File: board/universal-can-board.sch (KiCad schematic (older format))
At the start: 57 parts, among them IC1 ATMEGA328P-A, P1 USB_OTG, U1 FT232RL

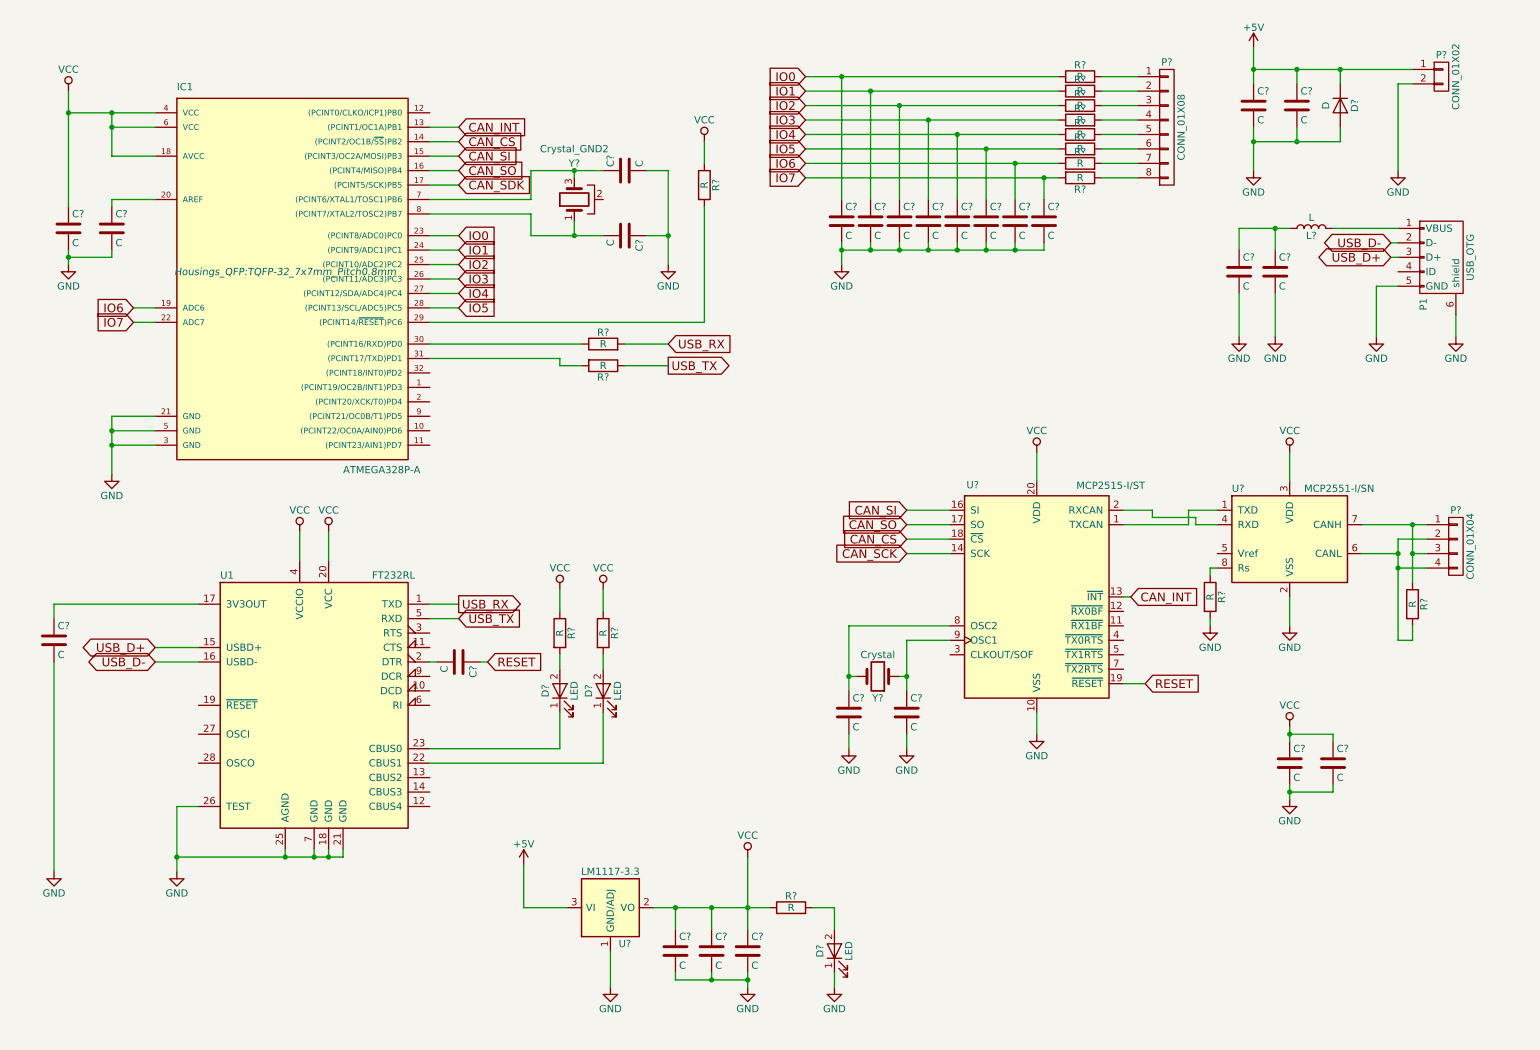
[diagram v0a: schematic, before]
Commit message: Added values to the board schematic.
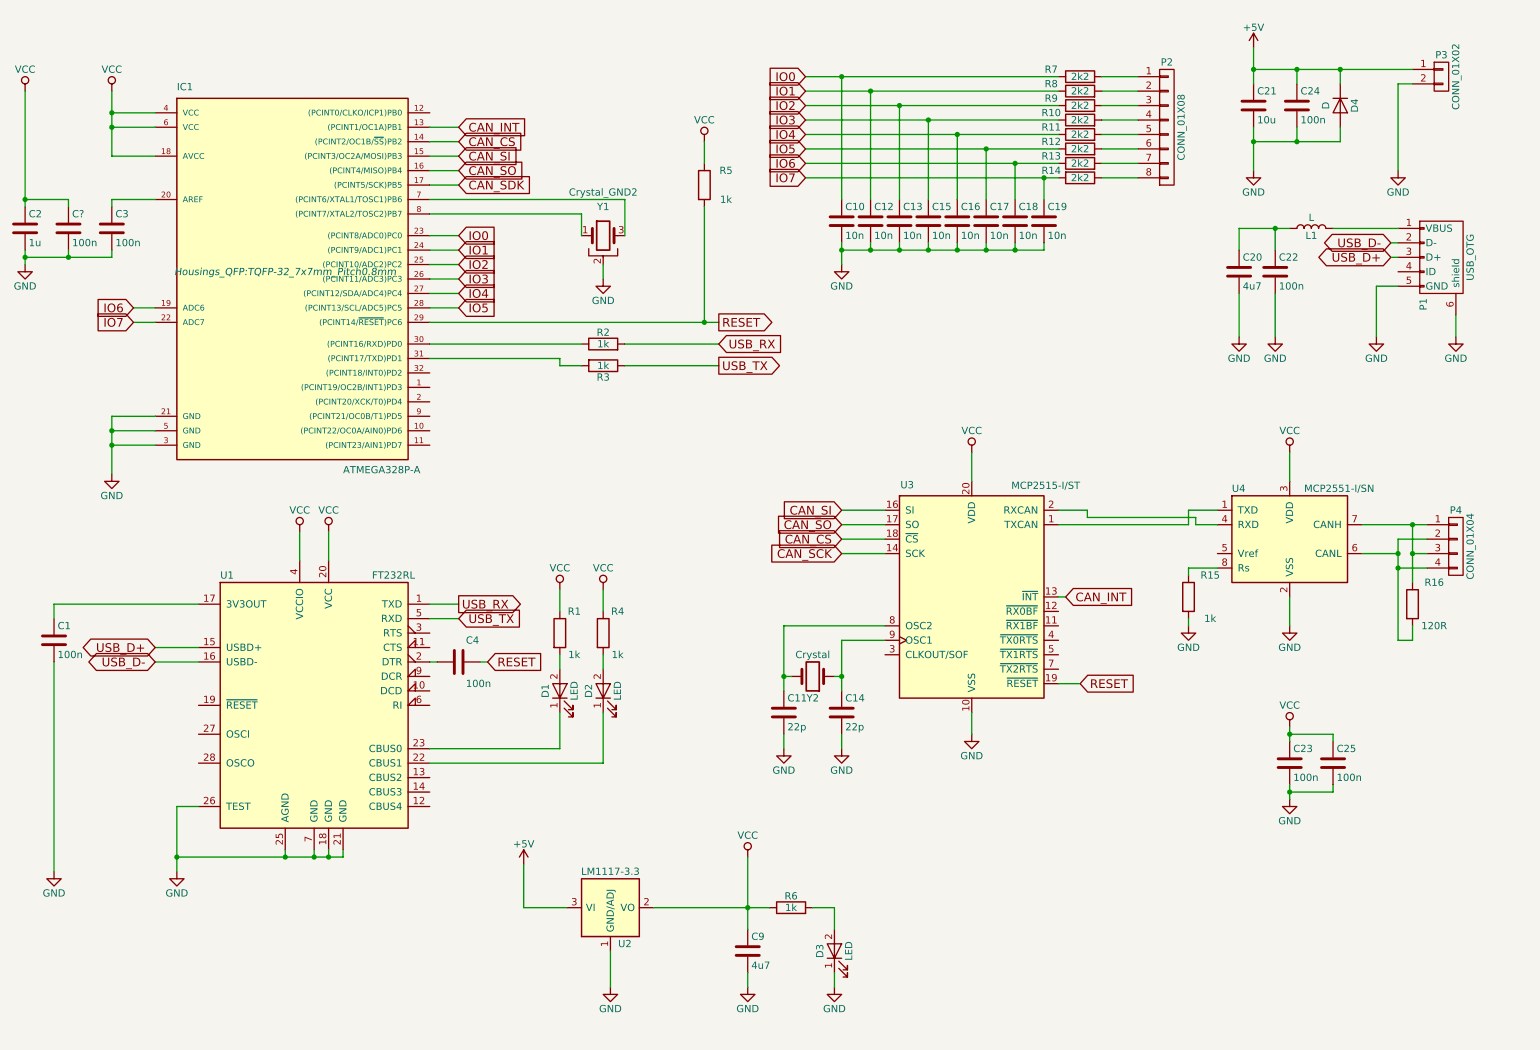
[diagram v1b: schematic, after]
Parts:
- removed C? (x4): C, symbol C
- added C?: 100n, symbol C
- C1, C22, C23, C24, C25, C3, C4: renamed from C?; value C -> 100n
- C10, C12, C13, C15, C16, C17, C18, C19: renamed from C?; value C -> 10n
- C11, C14: renamed from C?; value C -> 22p
- C2: renamed from C?; value C -> 1u
- C20, C9: renamed from C?; value C -> 4u7
- C21: renamed from C?; value C -> 10u
- R1, R15, R2, R3, R4, R5, R6: renamed from R?; value R -> 1k
- R10, R11, R12, R13, R14, R7, R8, R9: renamed from R?; value R -> 2k2
- R16: renamed from R?; value R -> 120R
- gave numbers to parts that had none: 13
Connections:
- net GND: now also Y1.2, C?.2
- net RESET: now also IC1.29 ((PCINT14/~RESET~)PC6), R5.2
- net VCC: now also C?.1
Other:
- moved on the sheet: C11, C14, C2, R15, U3, Y1, Y2

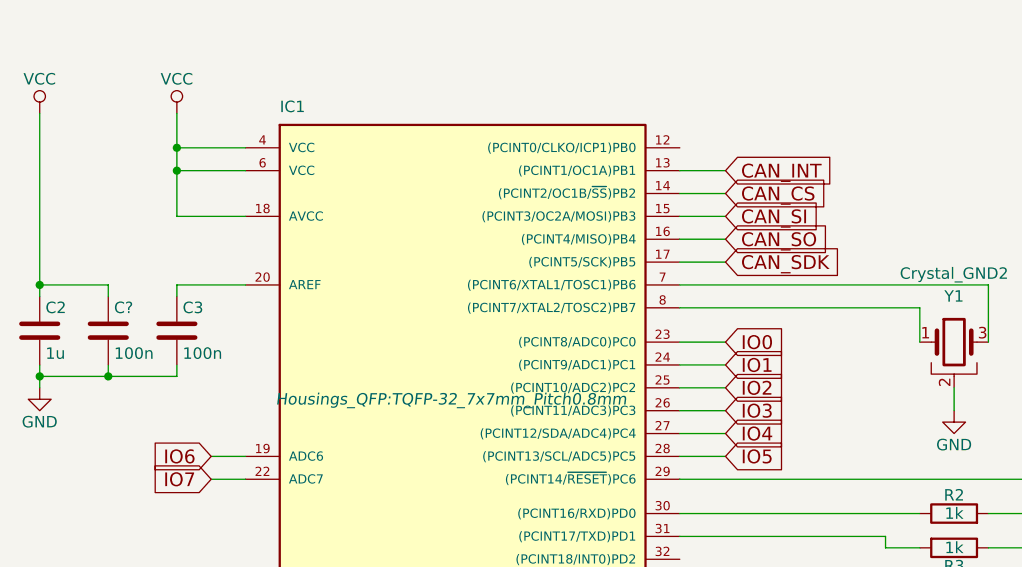
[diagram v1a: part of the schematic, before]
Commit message: Removed conflicts in board schematic.
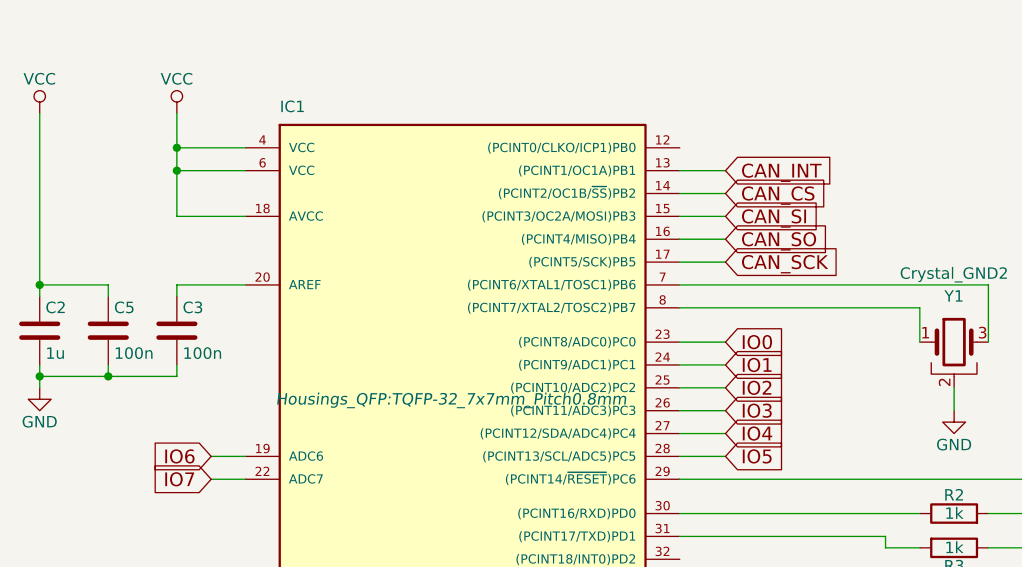
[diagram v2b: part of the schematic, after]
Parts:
- gave numbers to parts that had none: 1
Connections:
- net CAN_SDK is gone; now on net CAN_SCK: IC1.17 ((PCINT5/SCK)PB5)
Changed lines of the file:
@@
 $EndComp
 $Comp
-L GND #PWR4
+L GND #PWR01
 U 1 1 5A6CF0D9
 P 1350 3700
-F 0 "#PWR4" H 1350 3450 50  0001 C CNN
+F 0 "#PWR01" H 1350 3450 50  0001 C CNN
 F 1 "GND" H 1350 3550 50  0000 C CNN
 F 2 "" H 1350 3700 50  0000 C CNN
@@
 	750  1050 750  1850
 $Comp
-L GND #PWR3
+L GND #PWR02
 U 1 1 5A6CF36D
 P 750 2250
-F 0 "#PWR3" H 750 2000 50  0001 C CNN
+F 0 "#PWR02" H 750 2000 50  0001 C CNN
 F 1 "GND" H 750 2100 50  0000 C CNN
 F 2 "" H 750 2250 50  0000 C CNN
@@
 Connection ~ 750  2200
 $Comp
-L VCC #PWR2
+L VCC #PWR03
 U 1 1 5A6CF8D1
 P 750 1050
-F 0 "#PWR2" H 750 900 50  0001 C CNN
+F 0 "#PWR03" H 750 900 50  0001 C CNN
 F 1 "VCC" H 750 1200 50  0000 C CNN
 F 2 "" H 750 1050 50  0000 C CNN
@@
 	5450 1850 5450 2650
 $Comp
-L VCC #PWR13
+L VCC #PWR04
 U 1 1 5A6CFAE4
 P 5450 1400
-F 0 "#PWR13" H 5450 1250 50  0001 C CNN
+F 0 "#PWR04" H 5450 1250 50  0001 C CNN
 F 1 "VCC" H 5450 1550 50  0000 C CNN
 F 2 "" H 5450 1400 50  0000 C CNN
@@
 $EndComp
 $Comp
-L GND #PWR11
+L GND #PWR05
 U 1 1 5A6D0725
 P 4800 7250
-F 0 "#PWR11" H 4800 7000 50  0001 C CNN
+F 0 "#PWR05" H 4800 7000 50  0001 C CNN
 F 1 "GND" H 4800 7100 50  0000 C CNN
 F 2 "" H 4800 7250 50  0000 C CNN
@@
 	4800 7250 4800 7000
 $Comp
-L +5V #PWR8
+L +5V #PWR06
 U 1 1 5A6D0796
 P 4200 6400
-F 0 "#PWR8" H 4200 6250 50  0001 C CNN
+F 0 "#PWR06" H 4200 6250 50  0001 C CNN
 F 1 "+5V" H 4200 6540 50  0000 C CNN
 F 2 "" H 4200 6400 50  0000 C CNN
@@
 	4200 6400 4200 6700
 $Comp
-L VCC #PWR14
+L VCC #PWR07
 U 1 1 5A6D09D0
 P 5750 6350
-F 0 "#PWR14" H 5750 6200 50  0001 C CNN
+F 0 "#PWR07" H 5750 6200 50  0001 C CNN
 F 1 "VCC" H 5750 6500 50  0000 C CNN
 F 2 "" H 5750 6350 50  0000 C CNN
@@
 Connection ~ 5750 6700
 Wire Wire Line
-	5100 6700 5900 6700
-Wire Wire Line
 	5750 7150 5750 7250
 $Comp
-L GND #PWR15
+L GND #PWR08
 U 1 1 5A6D0D86
 P 5750 7250
-F 0 "#PWR15" H 5750 7000 50  0001 C CNN
+F 0 "#PWR08" H 5750 7000 50  0001 C CNN
 F 1 "GND" H 5750 7100 50  0000 C CNN
 F 2 "" H 5750 7250 50  0000 C CNN
@@
 	6350 6700 6350 6850
 $Comp
-L GND #PWR16
+L GND #PWR09
 U 1 1 5A6D152D
 P 6350 7250
-F 0 "#PWR16" H 6350 7000 50  0001 C CNN
+F 0 "#PWR09" H 6350 7000 50  0001 C CNN
 F 1 "GND" H 6350 7100 50  0000 C CNN
 F 2 "" H 6350 7250 50  0000 C CNN
@@
 $EndComp
 $Comp
-L GND #PWR25
+L GND #PWR010
 U 1 1 5A6D1F72
 P 9250 1600
-F 0 "#PWR25" H 9250 1350 50  0001 C CNN
+F 0 "#PWR010" H 9250 1350 50  0001 C CNN
 F 1 "GND" H 9250 1450 50  0000 C CNN
 F 2 "" H 9250 1600 50  0000 C CNN
@@
 Connection ~ 9550 1400
 $Comp
-L GND #PWR32
+L GND #PWR011
 U 1 1 5A6D222F
 P 10250 1600
-F 0 "#PWR32" H 10250 1350 50  0001 C CNN
+F 0 "#PWR011" H 10250 1350 50  0001 C CNN
 F 1 "GND" H 10250 1450 50  0000 C CNN
 F 2 "" H 10250 1600 50  0000 C CNN
@@
 	10250 1000 10350 1000
 $Comp
-L +5V #PWR24
+L +5V #PWR012
 U 1 1 5A6D22D2
 P 9250 750
-F 0 "#PWR24" H 9250 600 50  0001 C CNN
+F 0 "#PWR012" H 9250 600 50  0001 C CNN
 F 1 "+5V" H 9250 890 50  0000 C CNN
 F 2 "" H 9250 750 50  0000 C CNN
@@
 	9800 2000 10250 2000
 $Comp
-L GND #PWR31
+L GND #PWR013
 U 1 1 5A6D5AAC
 P 10100 2750
-F 0 "#PWR31" H 10100 2500 50  0001 C CNN
+F 0 "#PWR013" H 10100 2500 50  0001 C CNN
 F 1 "GND" H 10100 2600 50  0000 C CNN
 F 2 "" H 10100 2750 50  0000 C CNN
@@
 	10650 2600 10650 2750
 $Comp
-L GND #PWR33
+L GND #PWR014
 U 1 1 5A6D5D80
 P 10650 2750
-F 0 "#PWR33" H 10650 2500 50  0001 C CNN
+F 0 "#PWR014" H 10650 2500 50  0001 C CNN
 F 1 "GND" H 10650 2600 50  0000 C CNN
 F 2 "" H 10650 2750 50  0000 C CNN
@@
 Connection ~ 9400 2000
 $Comp
-L GND #PWR26
+L GND #PWR015
 U 1 1 5A6D64CB
 P 9400 2750
-F 0 "#PWR26" H 9400 2500 50  0001 C CNN
+F 0 "#PWR015" H 9400 2500 50  0001 C CNN
 F 1 "GND" H 9400 2600 50  0000 C CNN
 F 2 "" H 9400 2750 50  0000 C CNN
@@
 $EndComp
 $Comp
-L GND #PWR23
+L GND #PWR016
 U 1 1 5A6D655D
 P 9150 2750
-F 0 "#PWR23" H 9150 2500 50  0001 C CNN
+F 0 "#PWR016" H 9150 2500 50  0001 C CNN
 F 1 "GND" H 9150 2600 50  0000 C CNN
 F 2 "" H 9150 2750 50  0000 C CNN
@@
 	1650 4900 1950 4900
 $Comp
-L GND #PWR5
+L GND #PWR017
 U 1 1 5A6D83A0
 P 1800 6450
-F 0 "#PWR5" H 1800 6200 50  0001 C CNN
+F 0 "#PWR017" H 1800 6200 50  0001 C CNN
 F 1 "GND" H 1800 6300 50  0000 C CNN
 F 2 "" H 1800 6450 50  0000 C CNN
@@
 	4750 5700 3550 5700
 $Comp
-L VCC #PWR9
+L VCC #PWR018
 U 1 1 5A6D92A9
 P 4450 4500
-F 0 "#PWR9" H 4450 4350 50  0001 C CNN
+F 0 "#PWR018" H 4450 4350 50  0001 C CNN
 F 1 "VCC" H 4450 4650 50  0000 C CNN
 F 2 "" H 4450 4500 50  0000 C CNN
@@
 $EndComp
 $Comp
-L VCC #PWR10
+L VCC #PWR019
 U 1 1 5A6D931B
 P 4750 4500
-F 0 "#PWR10" H 4750 4350 50  0001 C CNN
+F 0 "#PWR019" H 4750 4350 50  0001 C CNN
 F 1 "VCC" H 4750 4650 50  0000 C CNN
 F 2 "" H 4750 4500 50  0000 C CNN
@@
 	4750 4500 4750 4650
 $Comp
-L VCC #PWR6
+L VCC #PWR020
 U 1 1 5A6D985E
 P 2650 4100
-F 0 "#PWR6" H 2650 3950 50  0001 C CNN
+F 0 "#PWR020" H 2650 3950 50  0001 C CNN
 F 1 "VCC" H 2650 4250 50  0000 C CNN
 F 2 "" H 2650 4100 50  0000 C CNN
@@
 $EndComp
 $Comp
-L VCC #PWR7
+L VCC #PWR021
 U 1 1 5A6D98D0
 P 2850 4100
-F 0 "#PWR7" H 2850 3950 50  0001 C CNN
+F 0 "#PWR021" H 2850 3950 50  0001 C CNN
 F 1 "VCC" H 2850 4250 50  0000 C CNN
 F 2 "" H 2850 4100 50  0000 C CNN
@@
 	2850 4100 2850 4300
 $Comp
-L GND #PWR1
+L GND #PWR022
 U 1 1 5A6D9C24
 P 950 6450
-F 0 "#PWR1" H 950 6200 50  0001 C CNN
+F 0 "#PWR022" H 950 6200 50  0001 C CNN
 F 1 "GND" H 950 6300 50  0000 C CNN
 F 2 "" H 950 6450 50  0000 C CNN
@@
 $EndComp
 $Comp
-L GND #PWR17
+L GND #PWR023
 U 1 1 5A6D2C05
 P 6400 2250
-F 0 "#PWR17" H 6400 2000 50  0001 C CNN
+F 0 "#PWR023" H 6400 2000 50  0001 C CNN
 F 1 "GND" H 6400 2100 50  0000 C CNN
 F 2 "" H 6400 2250 50  0000 C CNN
@@
 	7800 2150 7800 2100
 Connection ~ 7600 2150
-Wire Wire Line
-	4200 6700 4500 6700
 $Comp
 L MCP2515-I/ST U3
@@
 Connection ~ 10250 4350
 $Comp
-L GND #PWR28
+L GND #PWR024
 U 1 1 5A6D6414
 P 9500 4750
-F 0 "#PWR28" H 9500 4500 50  0001 C CNN
+F 0 "#PWR024" H 9500 4500 50  0001 C CNN
 F 1 "GND" H 9500 4600 50  0000 C CNN
 F 2 "" H 9500 4750 50  0000 C CNN
@@
 	9500 4750 9500 4550
 $Comp
-L GND #PWR21
+L GND #PWR025
 U 1 1 5A6D657F
 P 7300 5500
-F 0 "#PWR21" H 7300 5250 50  0001 C CNN
+F 0 "#PWR025" H 7300 5250 50  0001 C CNN
 F 1 "GND" H 7300 5350 50  0000 C CNN
 F 2 "" H 7300 5500 50  0000 C CNN
@@
 	7300 5500 7300 5350
 $Comp
-L VCC #PWR27
+L VCC #PWR026
 U 1 1 5A6D67EA
 P 9500 3550
-F 0 "#PWR27" H 9500 3400 50  0001 C CNN
+F 0 "#PWR026" H 9500 3400 50  0001 C CNN
 F 1 "VCC" H 9500 3700 50  0000 C CNN
 F 2 "" H 9500 3550 50  0000 C CNN
@@
 	9500 3550 9500 3750
 $Comp
-L VCC #PWR20
+L VCC #PWR027
 U 1 1 5A6D6957
 P 7300 3550
-F 0 "#PWR20" H 7300 3400 50  0001 C CNN
+F 0 "#PWR027" H 7300 3400 50  0001 C CNN
 F 1 "VCC" H 7300 3700 50  0000 C CNN
 F 2 "" H 7300 3550 50  0000 C CNN
@@
 	8800 4350 9000 4350
 $Comp
-L GND #PWR22
+L GND #PWR028
 U 1 1 5A6D6CE6
 P 8800 4750
-F 0 "#PWR22" H 8800 4500 50  0001 C CNN
+F 0 "#PWR028" H 8800 4500 50  0001 C CNN
 F 1 "GND" H 8800 4600 50  0000 C CNN
 F 2 "" H 8800 4750 50  0000 C CNN
@@
 Connection ~ 6000 5100
 $Comp
-L GND #PWR18
+L GND #PWR029
 U 1 1 5A6D8284
 P 6000 5600
-F 0 "#PWR18" H 6000 5350 50  0001 C CNN
+F 0 "#PWR029" H 6000 5350 50  0001 C CNN
 F 1 "GND" H 6000 5450 50  0000 C CNN
 F 2 "" H 6000 5600 50  0000 C CNN
@@
 $EndComp
 $Comp
-L GND #PWR19
+L GND #PWR030
 U 1 1 5A6D8306
 P 6400 5600
-F 0 "#PWR19" H 6400 5350 50  0001 C CNN
+F 0 "#PWR030" H 6400 5350 50  0001 C CNN
 F 1 "GND" H 6400 5450 50  0000 C CNN
 F 2 "" H 6400 5600 50  0000 C CNN
@@
 	1    0    0    -1
 $EndComp
-Wire Wire Line
-	6400 5600 6400 5500
 Wire Wire Line
 	6000 5600 6000 5500
@@
 $EndComp
 $Comp
-L GND #PWR30
+L GND #PWR031
 U 1 1 5A6DA852
 P 9500 5950
-F 0 "#PWR30" H 9500 5700 50  0001 C CNN
+F 0 "#PWR031" H 9500 5700 50  0001 C CNN
 F 1 "GND" H 9500 5800 50  0000 C CNN
 F 2 "" H 9500 5950 50  0000 C CNN
@@
 $EndComp
 $Comp
-L VCC #PWR29
+L VCC #PWR032
 U 1 1 5A6DA911
 P 9500 5450
-F 0 "#PWR29" H 9500 5300 50  0001 C CNN
+F 0 "#PWR032" H 9500 5300 50  0001 C CNN
 F 1 "VCC" H 9500 5600 50  0000 C CNN
 F 2 "" H 9500 5450 50  0000 C CNN
@@
 CAN_SO
 Text GLabel 3750 1700 2    60   Input ~ 0
-CAN_SDK
+CAN_SCK
 Wire Wire Line
 	3750 1500 3550 1500
 Wire Wire Line
 	3750 1600 3550 1600
-Wire Wire Line
-	3550 1700 3750 1700
 Text GLabel 3750 1400 2    60   Input ~ 0
 CAN_CS
@@
 	1500 2650 1650 2650
 $Comp
-L GND #PWR12
+L GND #PWR033
 U 1 1 5A6D02D7
 P 4750 2350
-F 0 "#PWR12" H 4750 2100 50  0001 C CNN
+F 0 "#PWR033" H 4750 2100 50  0001 C CNN
 F 1 "GND" H 4750 2200 50  0000 C CNN
 F 2 "" H 4750 2350 50  0000 C CNN
@@
 	8800 4350 8800 4400
 $Comp
-L C C?
+L C C5
 U 1 1 5A6F3843
 P 1050 2000
-F 0 "C?" H 1075 2100 50  0000 L CNN
+F 0 "C5" H 1075 2100 50  0000 L CNN
 F 1 "100n" H 1075 1900 50  0000 L CNN
 F 2 "" H 1088 1850 50  0000 C CNN
@@
 Connection ~ 750  1800
 $Comp
-L VCC #PWR?
+L VCC #PWR034
 U 1 1 5A6F43A8
 P 1350 1050
-F 0 "#PWR?" H 1350 900 50  0001 C CNN
+F 0 "#PWR034" H 1350 900 50  0001 C CNN
 F 1 "VCC" H 1350 1200 50  0000 C CNN
 F 2 "" H 1350 1050 50  0000 C CNN
@@
 	1350 1500 1650 1500
 Connection ~ 1350 1300
+Wire Wire Line
+	3550 1700 3750 1700
+Wire Wire Line
+	6400 5600 6400 5500
+Wire Wire Line
+	5100 6700 5900 6700
+Wire Wire Line
+	4200 6700 4500 6700
 $EndSCHEMATC
